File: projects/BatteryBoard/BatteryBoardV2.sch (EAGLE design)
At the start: 223 parts, among them M1 BSO201SP, SW1 BTS50015-1TAD, SW2 BTS50015-1TAD, T1 AD590FLATPACK, T2 AD590FLATPACK, T3 AD590FLATPACK, T4 AD590FLATPACK, U1 TCA9535PWR, U10 LT1962-3, U11 LT1962-3, U12 LTC4411, U13 LTC4411, U14 LTC4121, U15 VNS3NV04DP-E, U16 LTC4121, U17 VNS3NV04DP-E, U18 AD8418, U19 AD8418, U2 AD7991-0, U3 LTC4412MPS6, U4 LTC4121-4.2, U5 LTC4121-4.2, U6 LC05111C13MTTTG, U7 LC05111C13MTTTG, U8 AD8418, U9 AD8418

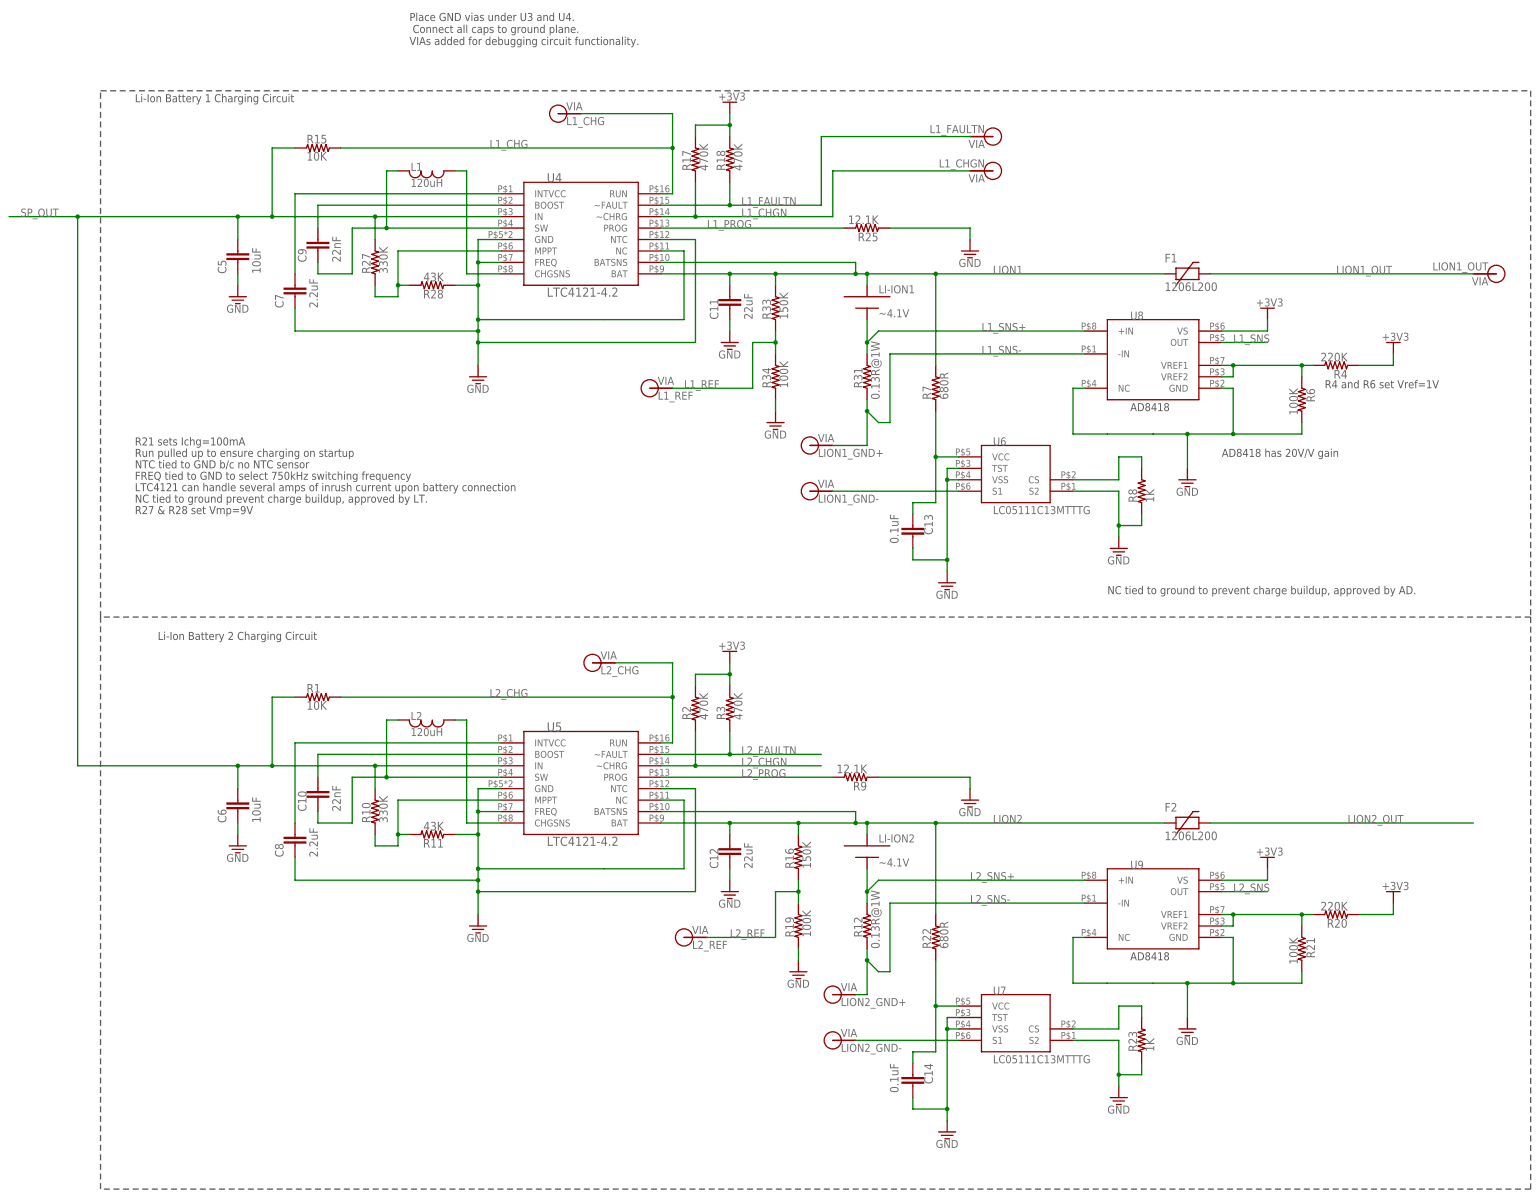
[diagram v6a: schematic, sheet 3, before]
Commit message: Continued routing of Battery Board V2. Addition of a few extra debugging vias. Addition of resistor dividers on li-ion charge commands.
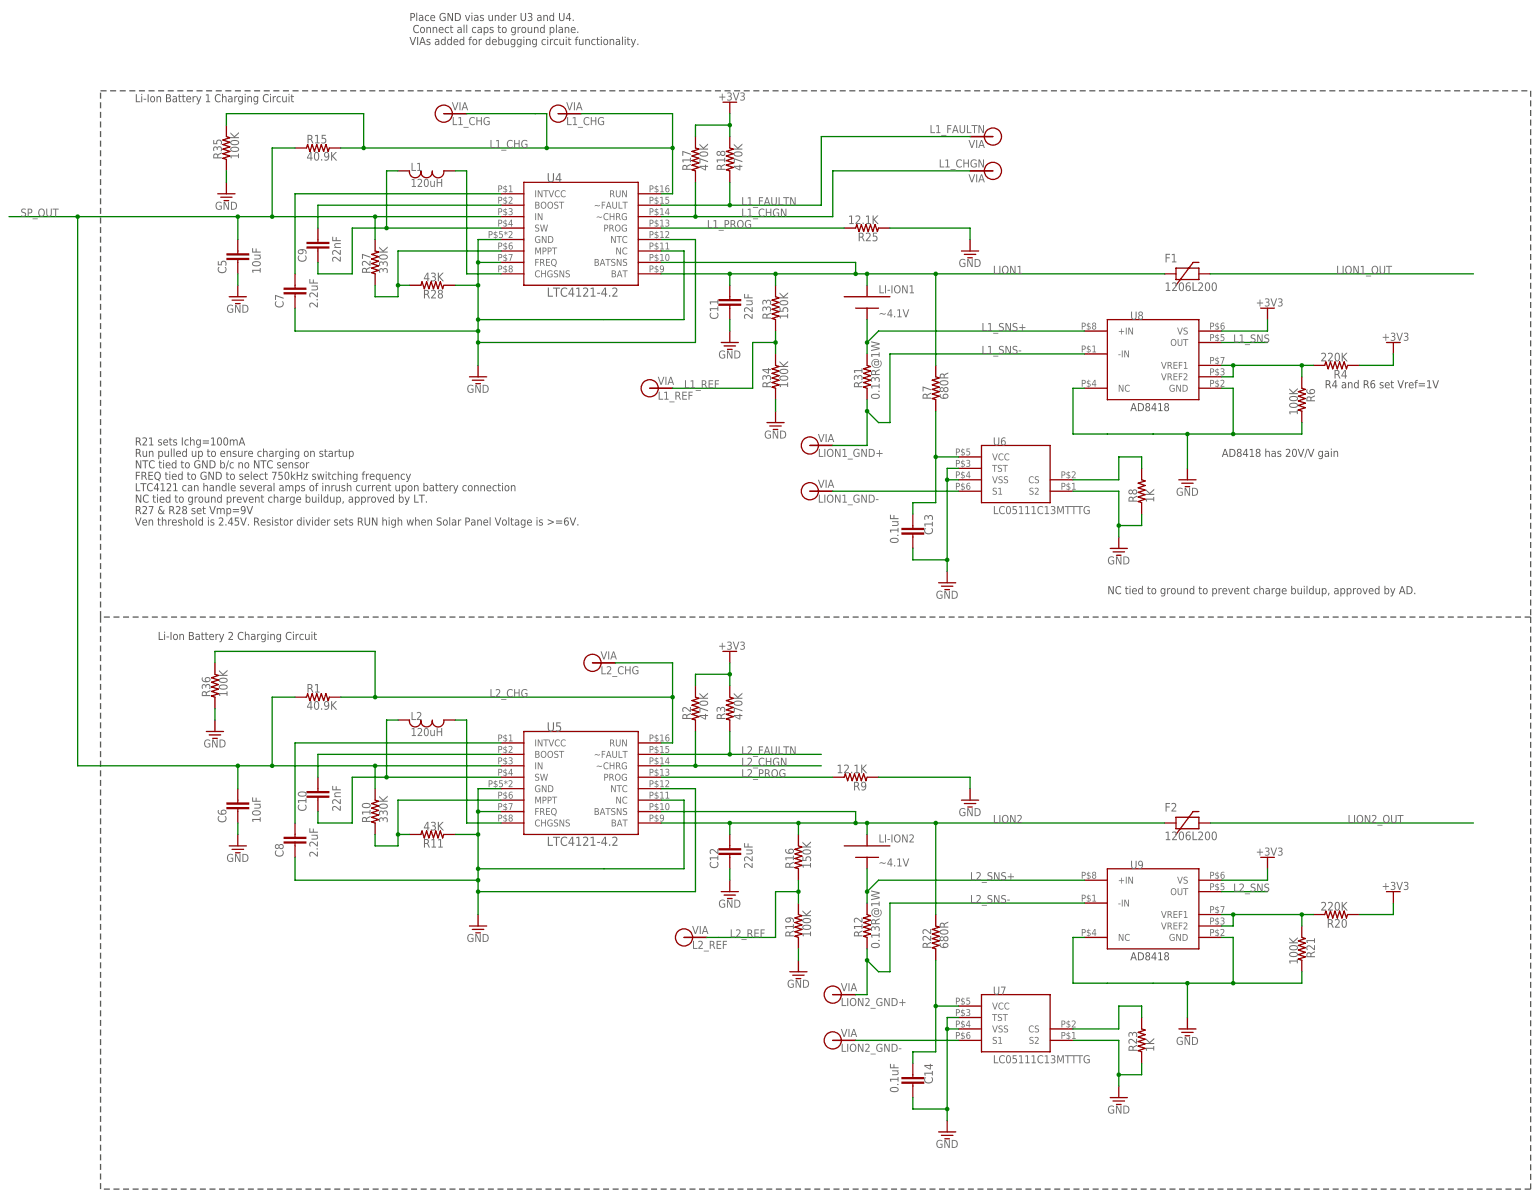
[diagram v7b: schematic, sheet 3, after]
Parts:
- removed V28: LION1_OUT, BrownSpaceEngineering:VIA60MIL-SQ
- added R32, R35, R36: 100K, BrownSpaceEngineering:RES0805
- added V32: LF_B1_CHG, BrownSpaceEngineering:VIA60MIL-SQ
- added V48: L1_CHG, BrownSpaceEngineering:VIA60MIL-SQ
- R1, R15: value 10K -> 40.9K
- V36, V37: device BrownSpaceEngineering:VIA-60MIL -> BrownSpaceEngineering:VIA60MIL-SQ
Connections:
- new net N$15: R32.2, U1.P03
- net GND: now also R32.1, R35.1, R36.1
- net L1_CHG: now also R35.2, V48.P$1
- net L2_CHG: now also R36.2
- net LF_B1_CHG: now also V32.P$1
- net LION1_OUT: no longer V28.P$1
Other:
- note added: "Place C5 near U3"
- note added: "Ven threshold is 2.45V. Resistor divider sets RUN high when Solar Panel Voltage is >=6V."
- note removed: "Place C3 near U3"
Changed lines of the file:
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@@
 <part name="GND7" library="supply1" deviceset="GND" device=""/>
 <part name="GND9" library="supply1" deviceset="GND" device=""/>
-<part name="R15" library="BrownSpaceEngineering" deviceset="RES" device="0805" value="10K"/>
+<part name="R15" library="BrownSpaceEngineering" deviceset="RES" device="0805" value="40.9K"/>
 <part name="R17" library="BrownSpaceEngineering" deviceset="RES" device="0805" value="470K"/>
 <part name="R18" library="BrownSpaceEngineering" deviceset="RES" device="0805" value="470K"/>
@@
 <part name="V39" library="BrownSpaceEngineering" deviceset="VIA" device="60MIL-SQ" value="LIFE2"/>
 <part name="V38" library="BrownSpaceEngineering" deviceset="VIA" device="60MIL-SQ" value="LIFE1"/>
-<part name="V36" library="BrownSpaceEngineering" deviceset="VIA" device="-60MIL" value="LF_B1_CHGN"/>
-<part name="V37" library="BrownSpaceEngineering" deviceset="VIA" device="-60MIL" value="LF_B1_FAULTN"/>
+<part name="V36" library="BrownSpaceEngineering" deviceset="VIA" device="60MIL-SQ" value="LF_B1_CHGN"/>
+<part name="V37" library="BrownSpaceEngineering" deviceset="VIA" device="60MIL-SQ" value="LF_B1_FAULTN"/>
 <part name="C28" library="BrownSpaceEngineering" deviceset="CAP" device="0805" value="22uF"/>
 <part name="U15" library="BrownSpaceEngineering" deviceset="VNS3NV04DP-E" device=""/>
@@
 <part name="V26" library="BrownSpaceEngineering" deviceset="VIA" device="60MIL-SQ" value="L1_FAULTN"/>
 <part name="V27" library="BrownSpaceEngineering" deviceset="VIA" device="60MIL-SQ" value="L1_CHGN"/>
-<part name="V28" library="BrownSpaceEngineering" deviceset="VIA" device="60MIL-SQ" value="LION1_OUT"/>
 <part name="T1" library="BrownSpaceEngineering" deviceset="AD590" device="FLATPACK"/>
 <part name="T2" library="BrownSpaceEngineering" deviceset="AD590" device="FLATPACK"/>
@@
 <part name="GND8" library="supply1" deviceset="GND" device=""/>
 <part name="GND10" library="supply1" deviceset="GND" device=""/>
-<part name="R1" library="BrownSpaceEngineering" deviceset="RES" device="0805" value="10K"/>
+<part name="R1" library="BrownSpaceEngineering" deviceset="RES" device="0805" value="40.9K"/>
 <part name="R2" library="BrownSpaceEngineering" deviceset="RES" device="0805" value="470K"/>
 <part name="R3" library="BrownSpaceEngineering" deviceset="RES" device="0805" value="470K"/>
@@
 <part name="V33" library="BrownSpaceEngineering" deviceset="VIA" device="-60MIL" value="L2_CHG"/>
 <part name="V31" library="BrownSpaceEngineering" deviceset="VIA" device="-60MIL" value="L2_REF"/>
+<part name="R32" library="BrownSpaceEngineering" deviceset="RES" device="0805" value="100K"/>
+<part name="GND55" library="supply1" deviceset="GND" device=""/>
+<part name="R35" library="BrownSpaceEngineering" deviceset="RES" device="0805" value="100K"/>
+<part name="GND56" library="supply1" deviceset="GND" device=""/>
+<part name="R36" library="BrownSpaceEngineering" deviceset="RES" device="0805" value="100K"/>
+<part name="GND57" library="supply1" deviceset="GND" device=""/>
+<part name="V32" library="BrownSpaceEngineering" deviceset="VIA" device="60MIL-SQ" value="LF_B1_CHG"/>
+<part name="V48" library="BrownSpaceEngineering" deviceset="VIA" device="60MIL-SQ" value="L1_CHG"/>
 </parts>
 <sheets>
@@
 <instance part="MTG3" gate="G$1" x="175.26" y="-7.62"/>
 <instance part="MTG4" gate="G$1" x="187.96" y="-7.62"/>
+<instance part="R32" gate="R$1" x="-15.24" y="60.96" rot="R90"/>
+<instance part="GND55" gate="1" x="-15.24" y="48.26"/>
 </instances>
 <busses>
@@
 <junction x="-88.9" y="38.1"/>
 </segment>
+<segment>
+<pinref part="R32" gate="R$1" pin="1"/>
+<pinref part="GND55" gate="1" pin="GND"/>
+<wire x1="-15.24" y1="55.88" x2="-15.24" y2="50.8" width="0.1524" layer="91"/>
+</segment>
 </net>
 <net name="5V" class="2">
@@
 <pinref part="+3V32" gate="G$1" pin="+3V3"/>
 <wire x1="91.44" y1="22.86" x2="91.44" y2="25.4" width="0.1524" layer="91"/>
+</segment>
+</net>
+<net name="N$15" class="0">
+<segment>
+<pinref part="U1" gate="G$1" pin="P03"/>
+<pinref part="R32" gate="R$1" pin="2"/>
+<wire x1="-48.26" y1="68.58" x2="-15.24" y2="68.58" width="0.1524" layer="91"/>
+<wire x1="-15.24" y1="68.58" x2="-15.24" y2="66.04" width="0.1524" layer="91"/>
 </segment>
 </net>
@@
 <text x="-58.42" y="40.64" size="1.778" layer="97">R21 sets Ichg=100mA</text>
 <text x="-58.42" y="25.4" size="1.778" layer="97">R27 &amp; R28 set Vmp=9V</text>
-<text x="-63.5" y="86.36" size="1.778" layer="98">Place C3 near U3</text>
+<text x="-60.96" y="88.9" size="1.778" layer="98">Place C5 near U3</text>
 <text x="-63.5" y="-53.34" size="1.778" layer="98">Place C5 near U4</text>
 <text x="-5.08" y="104.14" size="1.778" layer="98">Place L1 near SW pin</text>
@@
 as close as possible to R12</text>
 <text x="182.88" y="38.1" size="1.778" layer="97">AD8418 has 20V/V gain</text>
+<text x="-58.42" y="22.86" size="1.778" layer="97">Ven threshold is 2.45V. Resistor divider sets RUN high when Solar Panel Voltage is &gt;=6V.</text>
 </plain>
 <instances>
@@
 <instance part="V26" gate="G$1" x="132.08" y="109.22" rot="R180"/>
 <instance part="V27" gate="G$1" x="132.08" y="101.6" rot="R180"/>
-<instance part="V28" gate="G$1" x="243.84" y="78.74" rot="R180"/>
 <instance part="GND13" gate="1" x="83.82" y="45.72"/>
 <instance part="V22" gate="G$1" x="91.44" y="40.64"/>
@@
 <instance part="V33" gate="G$1" x="43.18" y="-7.62"/>
 <instance part="V31" gate="G$1" x="63.5" y="-68.58"/>
+<instance part="R35" gate="R$1" x="-38.1" y="106.68" rot="R90"/>
+<instance part="GND56" gate="1" x="-38.1" y="96.52"/>
+<instance part="R36" gate="R$1" x="-40.64" y="-12.7" rot="R90"/>
+<instance part="GND57" gate="1" x="-40.64" y="-22.86"/>
+<instance part="V48" gate="G$1" x="10.16" y="114.3"/>
 </instances>
 <busses>
@@
 <junction x="121.92" y="-106.68"/>
 </segment>
+<segment>
+<pinref part="GND56" gate="1" pin="GND"/>
+<pinref part="R35" gate="R$1" pin="1"/>
+<wire x1="-38.1" y1="99.06" x2="-38.1" y2="101.6" width="0.1524" layer="91"/>
+</segment>
+<segment>
+<pinref part="GND57" gate="1" pin="GND"/>
+<pinref part="R36" gate="R$1" pin="1"/>
+<wire x1="-40.64" y1="-20.32" x2="-40.64" y2="-17.78" width="0.1524" layer="91"/>
+</segment>
 </net>
 <net name="L1_CHGN" class="1">
@@
 <wire x1="58.42" y1="96.52" x2="60.96" y2="96.52" width="0.1524" layer="91"/>
 <wire x1="60.96" y1="96.52" x2="60.96" y2="106.68" width="0.1524" layer="91"/>
-<wire x1="60.96" y1="106.68" x2="-12.7" y2="106.68" width="0.1524" layer="91"/>
+<wire x1="60.96" y1="106.68" x2="33.02" y2="106.68" width="0.1524" layer="91"/>
 <pinref part="R15" gate="R$1" pin="2"/>
 <label x="20.32" y="106.68" size="1.778" layer="95"/>
 <pinref part="V20" gate="G$1" pin="P$1"/>
+<wire x1="33.02" y1="106.68" x2="-7.62" y2="106.68" width="0.1524" layer="91"/>
+<wire x1="-7.62" y1="106.68" x2="-12.7" y2="106.68" width="0.1524" layer="91"/>
 <wire x1="40.64" y1="114.3" x2="60.96" y2="114.3" width="0.1524" layer="91"/>
 <wire x1="60.96" y1="114.3" x2="60.96" y2="106.68" width="0.1524" layer="91"/>
 <junction x="60.96" y="106.68"/>
+<wire x1="-7.62" y1="106.68" x2="-7.62" y2="114.3" width="0.1524" layer="91"/>
+<junction x="-7.62" y="106.68"/>
+<pinref part="R35" gate="R$1" pin="2"/>
+<wire x1="-7.62" y1="114.3" x2="-38.1" y2="114.3" width="0.1524" layer="91"/>
+<wire x1="-38.1" y1="114.3" x2="-38.1" y2="111.76" width="0.1524" layer="91"/>
+<pinref part="V48" gate="G$1" pin="P$1"/>
+<wire x1="15.24" y1="114.3" x2="30.48" y2="114.3" width="0.1524" layer="91"/>
+<wire x1="30.48" y1="114.3" x2="33.02" y2="114.3" width="0.1524" layer="91"/>
+<wire x1="33.02" y1="114.3" x2="33.02" y2="106.68" width="0.1524" layer="91"/>
+<junction x="33.02" y="106.68"/>
 </segment>
 </net>
@@
 <wire x1="58.42" y1="-25.4" x2="60.96" y2="-25.4" width="0.1524" layer="91"/>
 <wire x1="60.96" y1="-25.4" x2="60.96" y2="-15.24" width="0.1524" layer="91"/>
-<wire x1="60.96" y1="-15.24" x2="-12.7" y2="-15.24" width="0.1524" layer="91"/>
+<wire x1="60.96" y1="-15.24" x2="-5.08" y2="-15.24" width="0.1524" layer="91"/>
 <pinref part="R1" gate="R$1" pin="2"/>
 <label x="20.32" y="-15.24" size="1.778" layer="95"/>
+<wire x1="-5.08" y1="-15.24" x2="-12.7" y2="-15.24" width="0.1524" layer="91"/>
 <wire x1="60.96" y1="-15.24" x2="60.96" y2="-7.62" width="0.1524" layer="91"/>
 <junction x="60.96" y="-15.24"/>
 <pinref part="V33" gate="G$1" pin="P$1"/>
 <wire x1="60.96" y1="-7.62" x2="48.26" y2="-7.62" width="0.1524" layer="91"/>
+<pinref part="R36" gate="R$1" pin="2"/>
+<wire x1="-40.64" y1="-7.62" x2="-40.64" y2="-5.08" width="0.1524" layer="91"/>
+<wire x1="-40.64" y1="-5.08" x2="-5.08" y2="-5.08" width="0.1524" layer="91"/>
+<wire x1="-5.08" y1="-5.08" x2="-5.08" y2="-15.24" width="0.1524" layer="91"/>
+<junction x="-5.08" y="-15.24"/>
 </segment>
 </net>
@@
 <segment>
 <pinref part="F1" gate="G$1" pin="P$2"/>
-<pinref part="V28" gate="G$1" pin="P$1"/>
 <wire x1="180.34" y1="78.74" x2="238.76" y2="78.74" width="0.1524" layer="91"/>
 <label x="208.28" y="78.74" size="1.778" layer="95"/>
@@
 <instance part="GND52" gate="1" x="218.44" y="17.78"/>
 <instance part="V40" gate="G$1" x="276.86" y="-30.48" rot="R180"/>
+<instance part="V32" gate="G$1" x="53.34" y="76.2"/>
 </instances>
 <busses>
@@
 <label x="78.74" y="83.82" size="1.778" layer="95"/>
 <pinref part="V35" gate="G$1" pin="P$1"/>
-<wire x1="58.42" y1="83.82" x2="78.74" y2="83.82" width="0.1524" layer="91"/>
+<wire x1="58.42" y1="83.82" x2="73.66" y2="83.82" width="0.1524" layer="91"/>
 <junction x="78.74" y="83.82"/>
-</segment>
-</net>
+<pinref part="V32" gate="G$1" pin="P$1"/>
+<wire x1="73.66" y1="83.82" x2="78.74" y2="83.82" width="0.1524" layer="91"/>
+<wire x1="58.42" y1="76.2" x2="73.66" y2="76.2" width="0.1524" layer="91"/>
+<wire x1="73.66" y1="76.2" x2="73.66" y2="83.82" width="0.1524" layer="91"/>
+<junction x="73.66" y="83.82"/>
+</segment>
+</net>
